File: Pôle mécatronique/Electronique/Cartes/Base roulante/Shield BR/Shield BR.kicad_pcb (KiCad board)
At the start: 2 copper layers, 66 x 61 mm, 40 parts, among them J1 Conn_01x04_Male, J2 Conn_01x04_Female, J3 Conn_01x04_Female, J4 Conn_01x04_Female, J5 Conn_01x04_Female, J5-CAN1 Conn_01x02_Female, SW1 SW_Push_SPDT, U1 R-78E5.0-0.5, U2 MCP2551-I-P

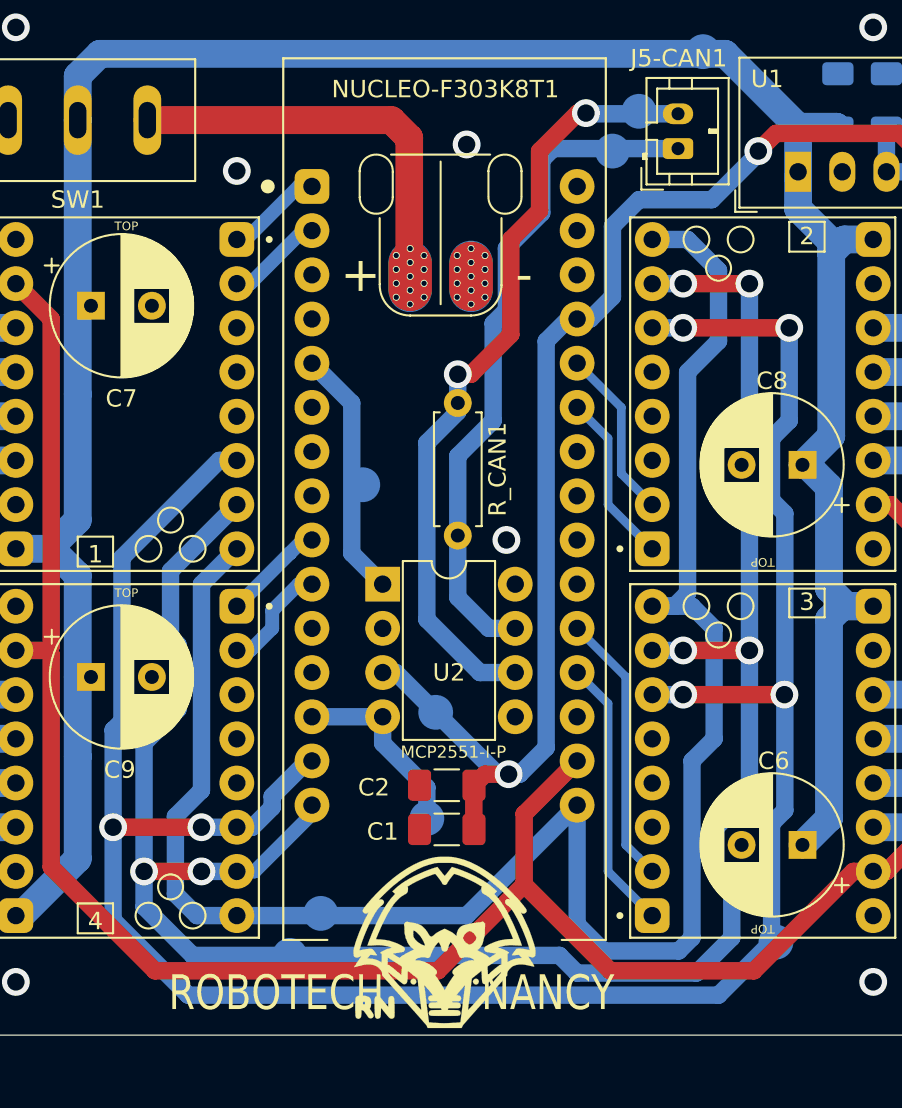
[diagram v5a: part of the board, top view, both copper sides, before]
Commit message: Udpate HAT
Sérigraphie
Points de tests
Arret d'urgence
I2C
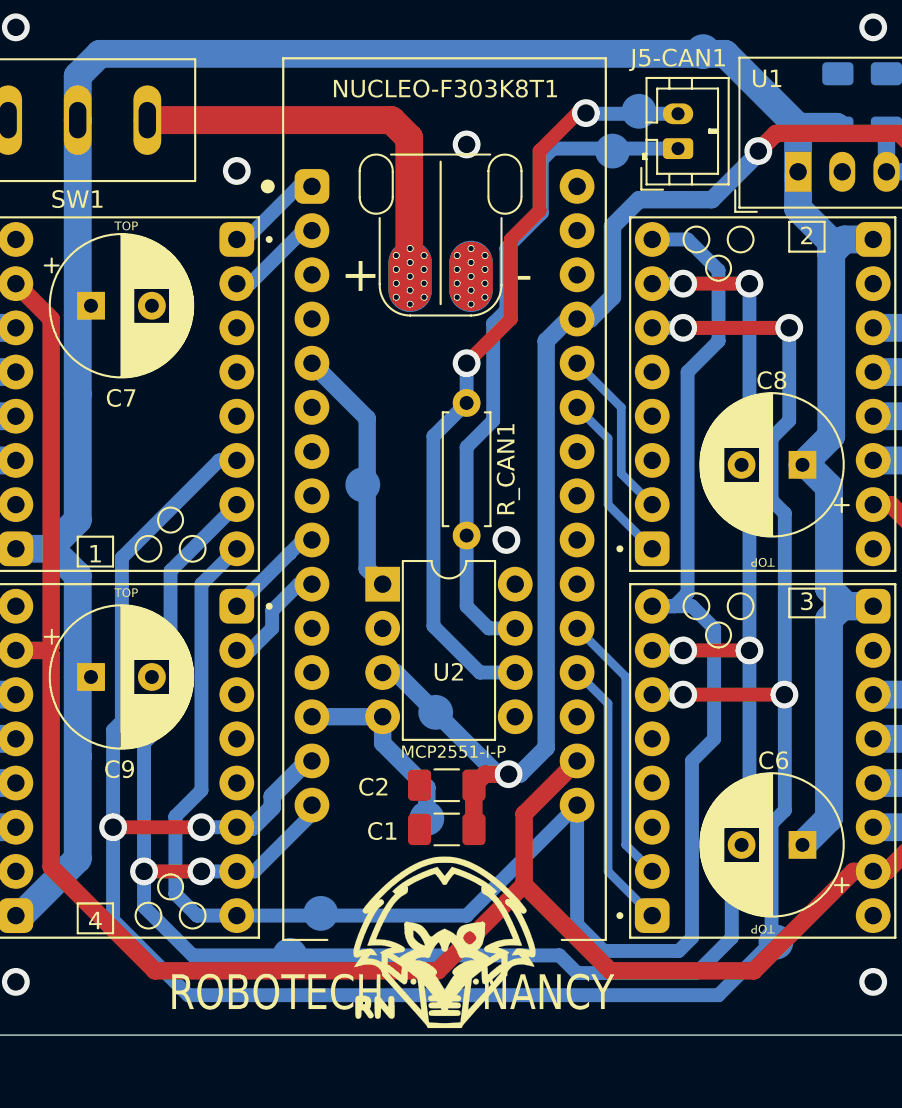
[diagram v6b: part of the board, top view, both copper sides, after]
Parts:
- moved R_CAN1 0.51 mm to (112.5, 96.0)
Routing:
- net Net-(J5-CAN1-Pad2): track 45.3 -> 44.5 mm

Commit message: Correction pcb BR
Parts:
- moved TP1 2.01 mm to (141.5, 72.6)
- moved SW1 0.64 mm to (90.8, 72.1)
- moved C1 0.38 mm to (111.0, 112.9)
- moved C2 0.38 mm to (111.0, 110.4)
- moved REF** 0.36 mm to (110.5, 105.9)
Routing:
- net GND: track 1.60 -> 22.3 mm, vias 20 -> 36
- net Vio: track 124.9 -> 140.2 mm, vias 0 -> 4
- net +5V: track 83.3 -> 86.8 mm
- net M1: track 125.1 -> 123.8 mm
- net M2: track 136.1 -> 135.2 mm
- net +BATT: track 151.8 -> 151.0 mm
- net Net-(J1-Pad1): track 25.1 -> 24.4 mm, vias 13 -> 14

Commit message: Minor changes
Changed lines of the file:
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@@
     (fp_circle (center 0 0) (end 1.75 0) (layer "Cmts.User") (width 0.15) (fill none))
     (fp_circle (center 0 0) (end 2 0) (layer "F.CrtYd") (width 0.05) (fill none))
-    (pad "" np_thru_hole circle locked (at 0 0) (size 2.2 2.2) (drill 2.2) (layers *.Cu *.Mask))
+    (pad "" np_thru_hole circle locked (at 0 0) (size 3.2 3.2) (drill 3.2) (layers F&B.Cu *.Mask))
   )
   (footprint "MountingHole:MountingHole_2.2mm_M2_ISO7380" (layer "F.Cu")
@@
     (fp_circle (center 0 0) (end 1.75 0) (layer "Cmts.User") (width 0.15) (fill none))
     (fp_circle (center 0 0) (end 2 0) (layer "F.CrtYd") (width 0.05) (fill none))
-    (pad "" np_thru_hole circle locked (at 0 0) (size 2.2 2.2) (drill 2.2) (layers *.Cu *.Mask))
+    (pad "" np_thru_hole circle locked (at 0 0) (size 3.2 3.2) (drill 3.2) (layers F&B.Cu *.Mask))
   )
   (footprint "MountingHole:MountingHole_2.2mm_M2_ISO7380" (layer "F.Cu")
@@
     (fp_circle (center 0 0) (end 1.75 0) (layer "Cmts.User") (width 0.15) (fill none))
     (fp_circle (center 0 0) (end 2 0) (layer "F.CrtYd") (width 0.05) (fill none))
-    (pad "" np_thru_hole circle locked (at 0 0) (size 2.2 2.2) (drill 2.2) (layers *.Cu *.Mask))
+    (pad "" np_thru_hole circle locked (at 0 0) (size 3.2 3.2) (drill 3.2) (layers F&B.Cu *.Mask))
   )
   (footprint "MountingHole:MountingHole_2.2mm_M2_ISO7380" (layer "F.Cu")
@@
     (fp_circle (center 0 0) (end 1.75 0) (layer "Cmts.User") (width 0.15) (fill none))
     (fp_circle (center 0 0) (end 2 0) (layer "F.CrtYd") (width 0.05) (fill none))
-    (pad "" np_thru_hole circle locked (at 0 0) (size 2.2 2.2) (drill 2.2) (layers *.Cu *.Mask))
+    (pad "" np_thru_hole circle locked (at 0 0) (size 3.2 3.2) (drill 3.2) (layers F&B.Cu *.Mask))
   )
   (footprint "Logos:logoRobotechNancy10x10" (layer "F.Cu")
@@
     (property "Sheetname" "")
     (attr smd)
-    (fp_text reference "C5" (at 3.4675 0 90) (layer "B.SilkS")
+    (fp_text reference "C5" (at 3.4675 -0.254 90) (layer "B.SilkS")
       (effects (font (size 1 1) (thickness 0.15)) (justify mirror))
     )
